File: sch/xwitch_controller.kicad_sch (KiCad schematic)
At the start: 28 parts

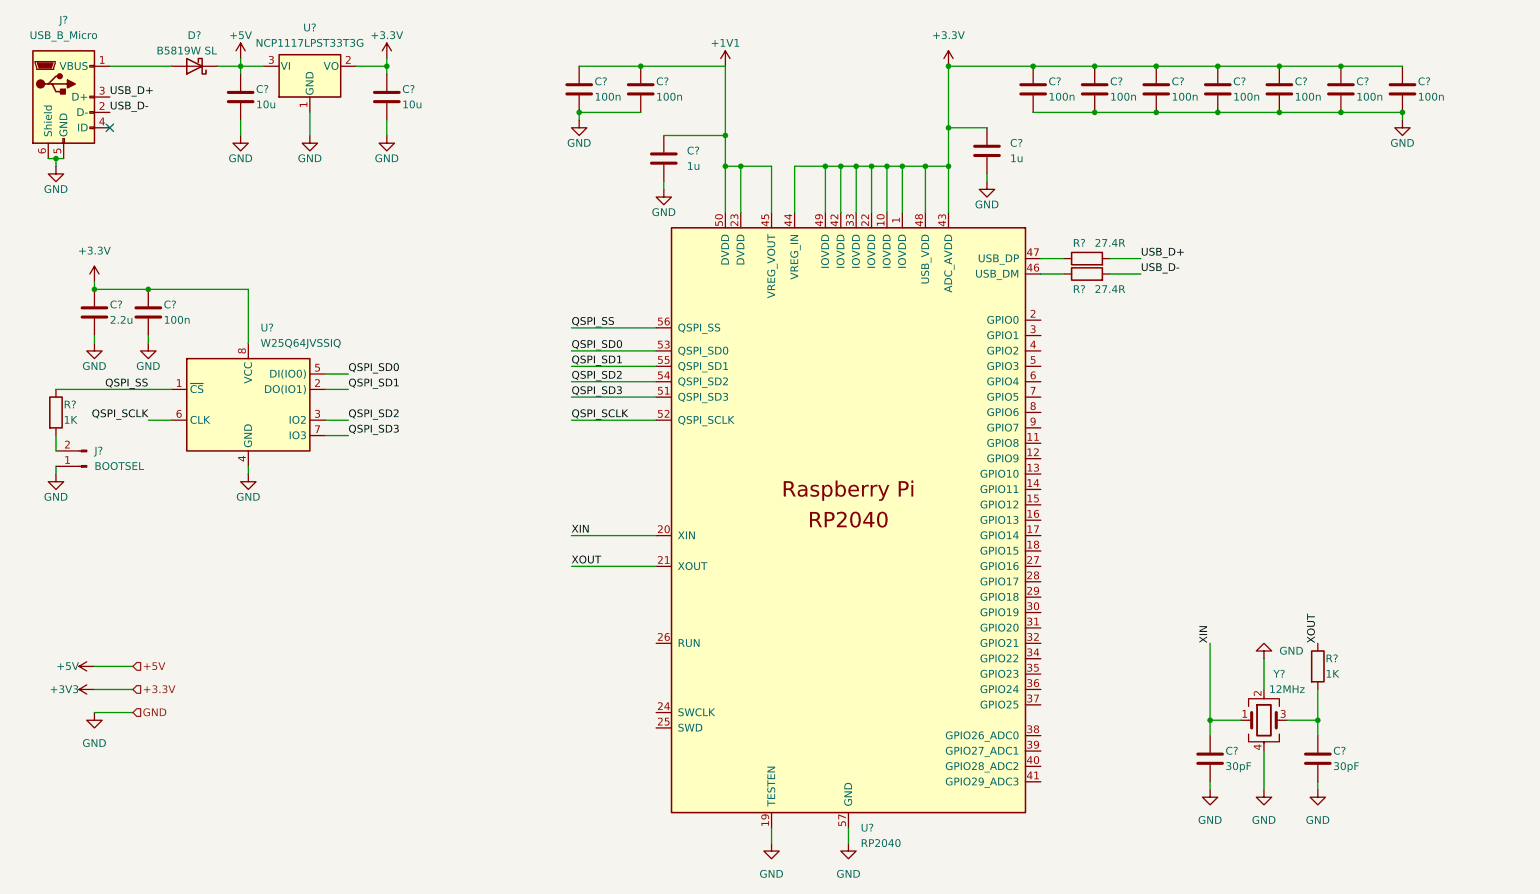
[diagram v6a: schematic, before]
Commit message: more  usb-c channels update
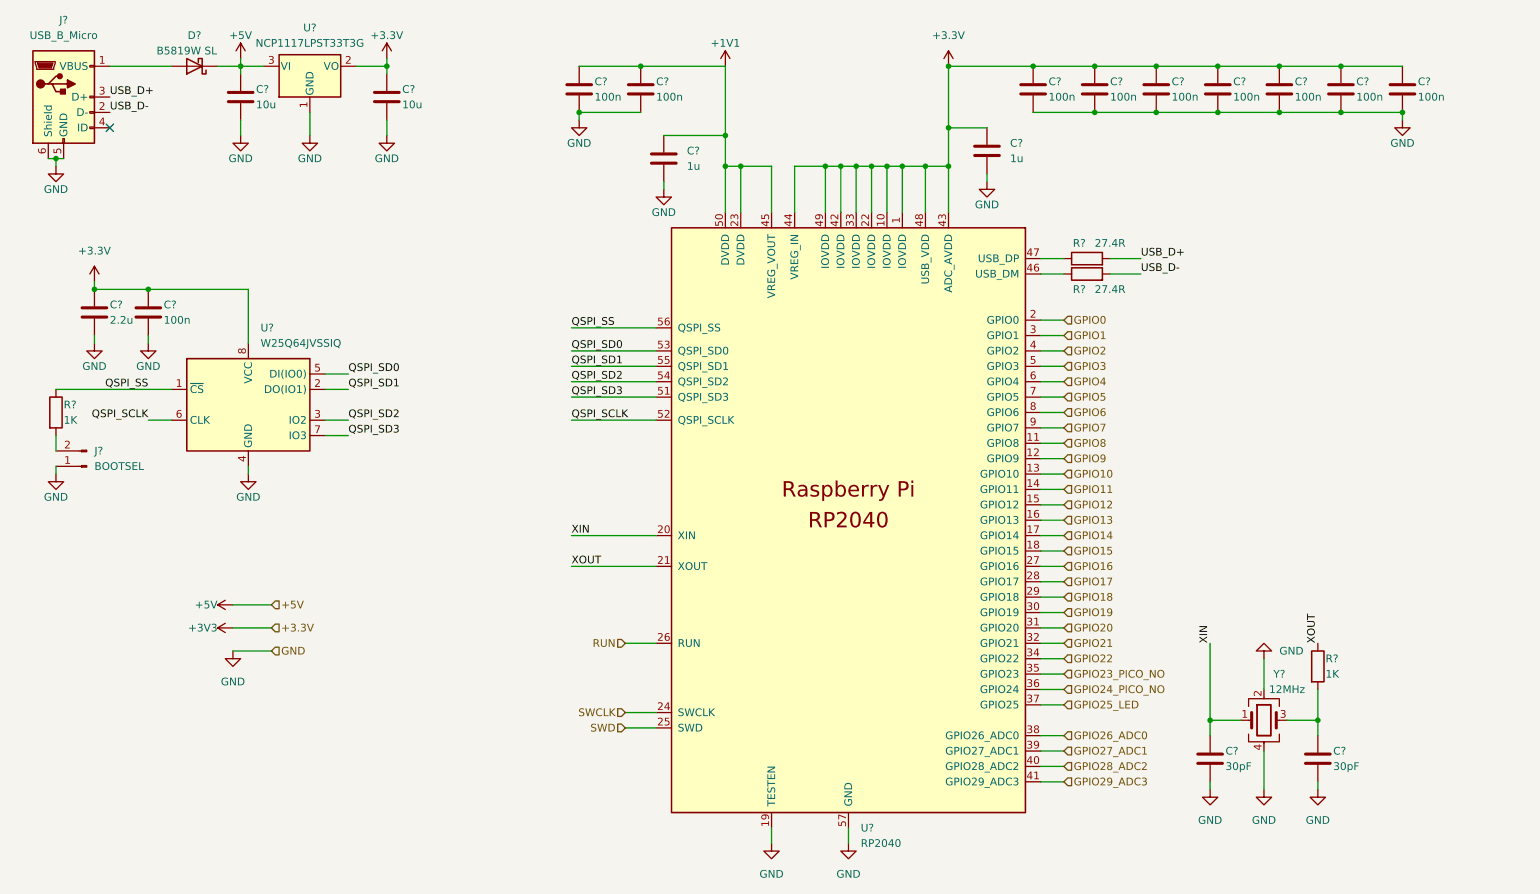
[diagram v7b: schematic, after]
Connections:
- net GPIO8: now reaches U?.11 (GPIO8)
- net GPIO9: now reaches U?.12 (GPIO9)
- net GPIO10: now reaches U?.13 (GPIO10)
- net GPIO11: now reaches U?.14 (GPIO11)
- net GPIO12: now reaches U?.15 (GPIO12)
- net GPIO13: now reaches U?.16 (GPIO13)
- net GPIO14: now reaches U?.17 (GPIO14)
- net GPIO15: now reaches U?.18 (GPIO15)
- net GPIO0: now reaches U?.2 (GPIO0)
- net SWCLK: now reaches U?.24 (SWCLK)
- net SWD: now reaches U?.25 (SWD)
- net RUN: now reaches U?.26 (RUN)
- net GPIO16: now reaches U?.27 (GPIO16)
- net GPIO17: now reaches U?.28 (GPIO17)
- net GPIO18: now reaches U?.29 (GPIO18)
- net GPIO1: now reaches U?.3 (GPIO1)
- net GPIO19: now reaches U?.30 (GPIO19)
- net GPIO20: now reaches U?.31 (GPIO20)
- net GPIO21: now reaches U?.32 (GPIO21)
- net GPIO22: now reaches U?.34 (GPIO22)
- net GPIO23_PICO_NO: now reaches U?.35 (GPIO23)
- net GPIO24_PICO_NO: now reaches U?.36 (GPIO24)
- net GPIO25_LED: now reaches U?.37 (GPIO25)
- net GPIO26_ADC0: now reaches U?.38 (GPIO26_ADC0)
- net GPIO27_ADC1: now reaches U?.39 (GPIO27_ADC1)
- net GPIO2: now reaches U?.4 (GPIO2)
- net GPIO28_ADC2: now reaches U?.40 (GPIO28_ADC2)
- net GPIO29_ADC3: now reaches U?.41 (GPIO29_ADC3)
- net GPIO3: now reaches U?.5 (GPIO3)
- net GPIO4: now reaches U?.6 (GPIO4)
- net GPIO5: now reaches U?.7 (GPIO5)
- net GPIO6: now reaches U?.8 (GPIO6)
- net GPIO7: now reaches U?.9 (GPIO7)

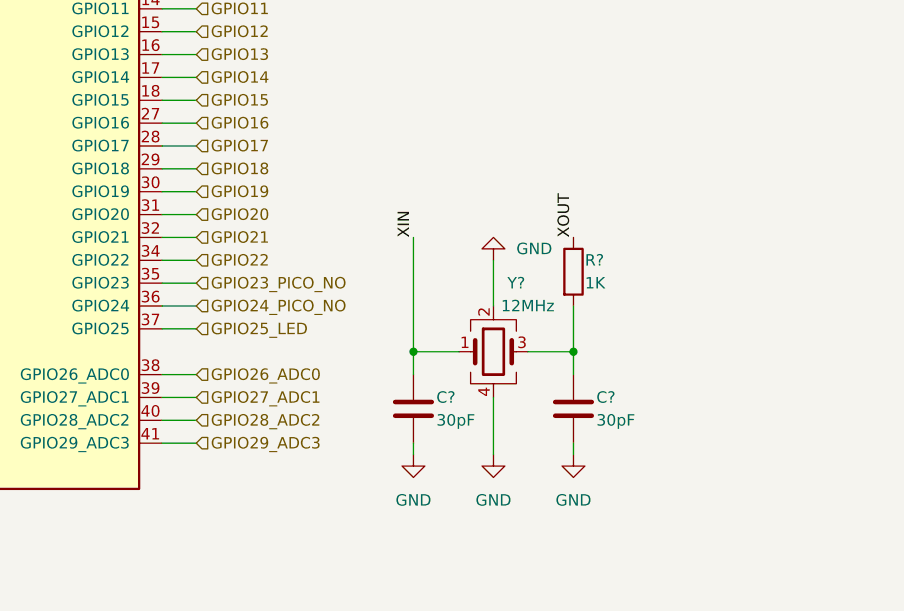
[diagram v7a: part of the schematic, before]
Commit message: replaced old pico board connection to embedded rp2040
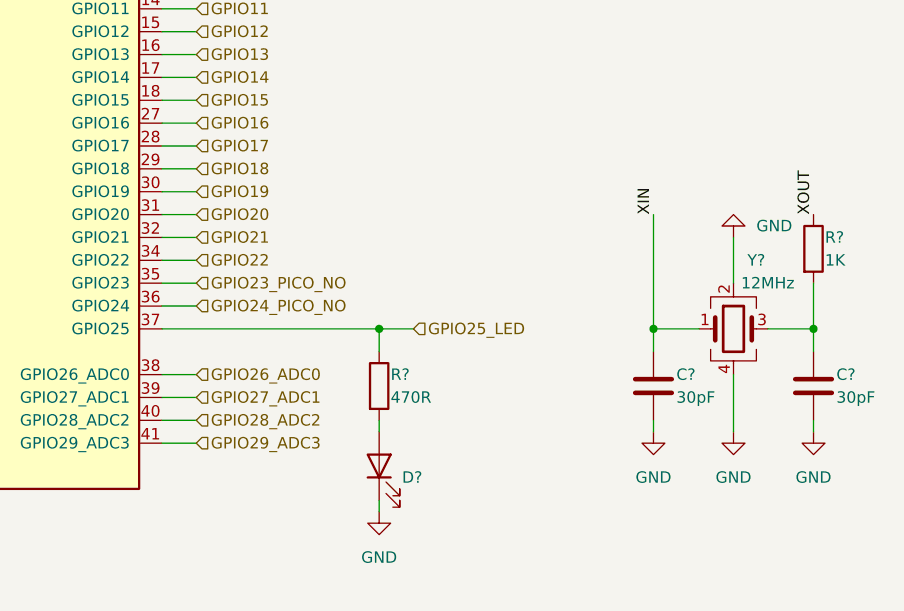
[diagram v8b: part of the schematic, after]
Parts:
- added D?: 19-217/GHC-YR1S2/3T, Diode_SMD:D_0603_1608Metric_Pad1.05x0.95mm_HandSolder, symbol Device:LED
- added R?: 470R, Resistor_SMD:R_0402_1005Metric_Pad0.72x0.64mm_HandSolder, symbol Device:R
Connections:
- net GND: now also D?.1 (K)
- net GPIO25_LED: now also R?.1
- new net: D?.2 (A), R?.2
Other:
- moved on the sheet: C?, R?, Y?
